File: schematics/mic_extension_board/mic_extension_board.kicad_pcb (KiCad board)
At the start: 2 copper layers, 103.5 x 88.9 mm, 56 parts, among them J1 XLR3, J2 Power, J3 Aux In, J4 I2C Bus, J5 6Pin ISP, J6 Input/Output, J7 XLR3, J8 XLR3, SW1 Stompbutton 1, SW2 Stompbutton 2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

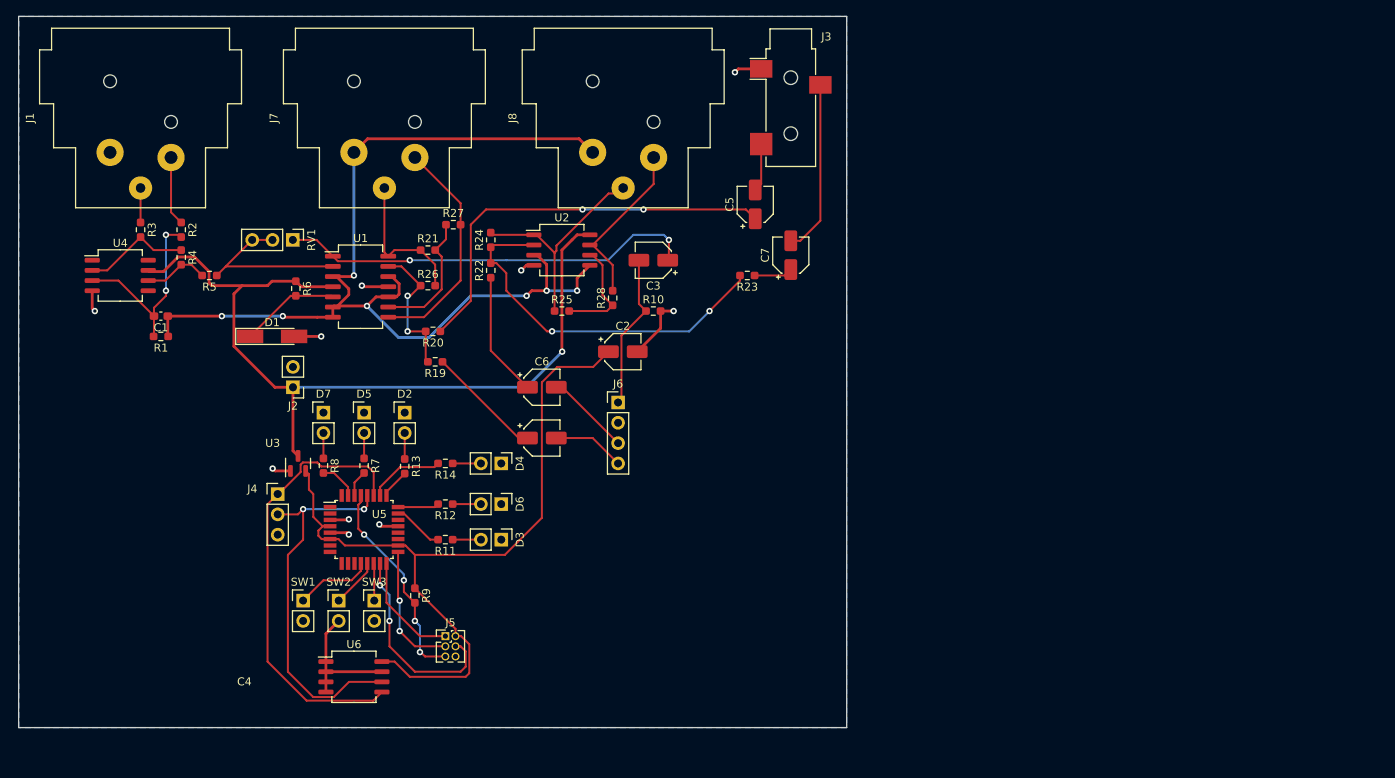
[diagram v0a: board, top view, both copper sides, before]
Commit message: corrected ic footprints, shrinked
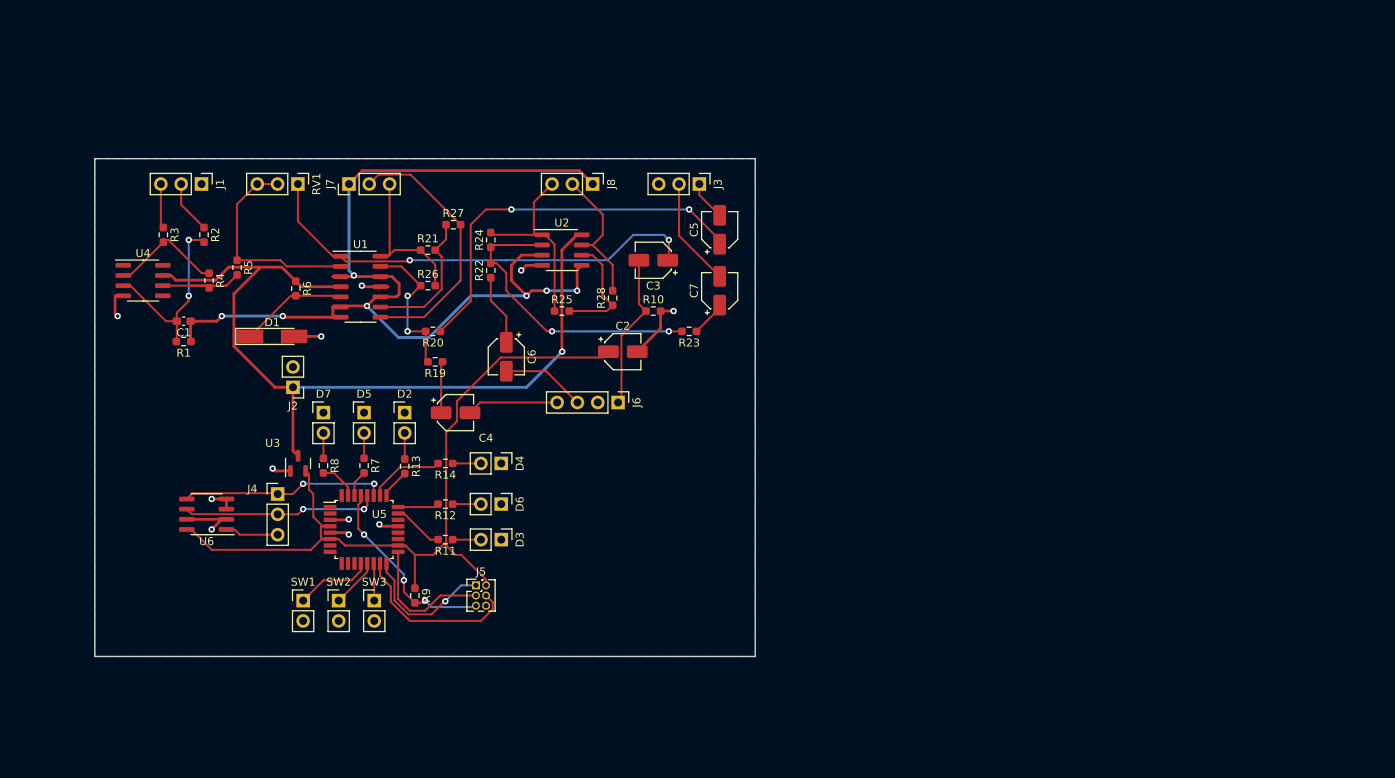
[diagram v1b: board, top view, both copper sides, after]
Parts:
- J1: footprint Connector_Audio:Jack_XLR_Neutrik_NC3FAAH-0_Horizontal -> Connector_PinHeader_2.54mm:PinHeader_1x03_P2.54mm_Vertical
- J3: footprint Connector_Audio:Jack_3.5mm_CUI_SJ-3523-SMT_Horizontal -> Connector_PinHeader_2.54mm:PinHeader_1x03_P2.54mm_Vertical
- J7, J8: footprint Connector_Audio:Jack_XLR_Neutrik_NC3FAAH1-0_Horizontal -> Connector_PinHeader_2.54mm:PinHeader_1x03_P2.54mm_Vertical
- U1: footprint Package_SO:SO-14_5.3x10.2mm_P1.27mm -> Package_SO:SOIC-14_3.9x8.7mm_P1.27mm
- U2, U4, U6: footprint Package_SO:SO-8_5.3x6.2mm_P1.27mm -> Package_SO:SOIC-8_3.9x4.9mm_P1.27mm
- moved U6 27.4 mm to (48.9, 72.4), turned to 180 degrees
- moved J3 15.7 mm to (110.5, 31.1), turned to -90 degrees
- moved J1 12.1 mm to (48.3, 31.1), turned to -90 degrees
- moved C4 11.3 mm to (80.0, 59.7)
- moved R23 10.1 mm to (109.2, 49.5)
- moved C7 9.94 mm to (113.0, 44.5)
- moved J5 7.41 mm to (82.6, 81.3)
- moved RV1 7.01 mm to (60.3, 31.1)
- moved C6 5.85 mm to (86.4, 52.7), turned to -90 degrees
- moved C5 5.46 mm to (113.0, 36.8)
- moved R4 4.53 mm to (49.2, 43.2)
- moved J7 4.00 mm to (66.7, 31.1)
- moved J8 3.95 mm to (97.2, 31.1), turned to -90 degrees
- moved R5 3.59 mm to (52.7, 41.6), turned to -90 degrees
- moved R2 2.92 mm to (48.6, 37.5)
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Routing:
- net Net-(J4-Pad1): track 55.8 -> 25.8 mm, vias 0 -> 2
- net Net-(J4-Pad2): track 47.9 -> 24.6 mm
- net Net-(R22-Pad2): track 46.7 -> 36.2 mm
- net Net-(C4-Pad1): track 14.6 -> 6.42 mm
- net Net-(C7-Pad2): track 21.7 -> 13.6 mm
- net Net-(C6-Pad1): track 15.6 -> 8.89 mm
- net Net-(J8-Pad3): track 28.6 -> 23.5 mm
- net GND: track 48.8 -> 44.3 mm, vias 10 -> 11
- net Net-(J8-Pad2): track 21.2 -> 16.8 mm
- net Net-(C3-Pad1): track 52.3 -> 56.4 mm
- net Vref: track 130.9 -> 127.1 mm
- net Net-(J7-Pad2): track 28.7 -> 32.4 mm
- net Net-(J5-Pad4): track 25.4 -> 21.7 mm, vias 2 -> 0
- net Net-(J5-Pad1): track 14.0 -> 17.6 mm, vias 0 -> 1
- net Net-(R4-Pad2): track 8.12 -> 11.4 mm
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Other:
- board size 103.5 x 88.9 mm -> 82.5 x 62.2 mm

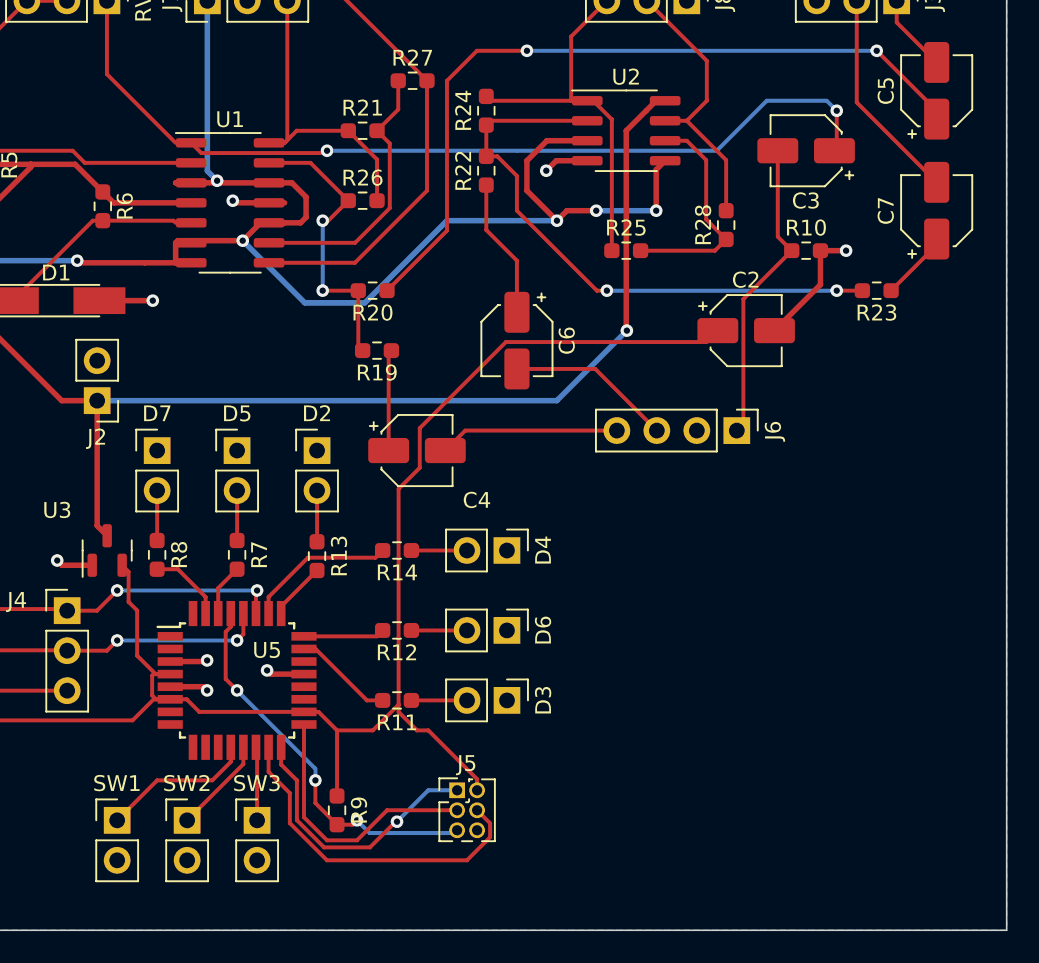
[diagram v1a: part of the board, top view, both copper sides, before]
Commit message: added headphone amp
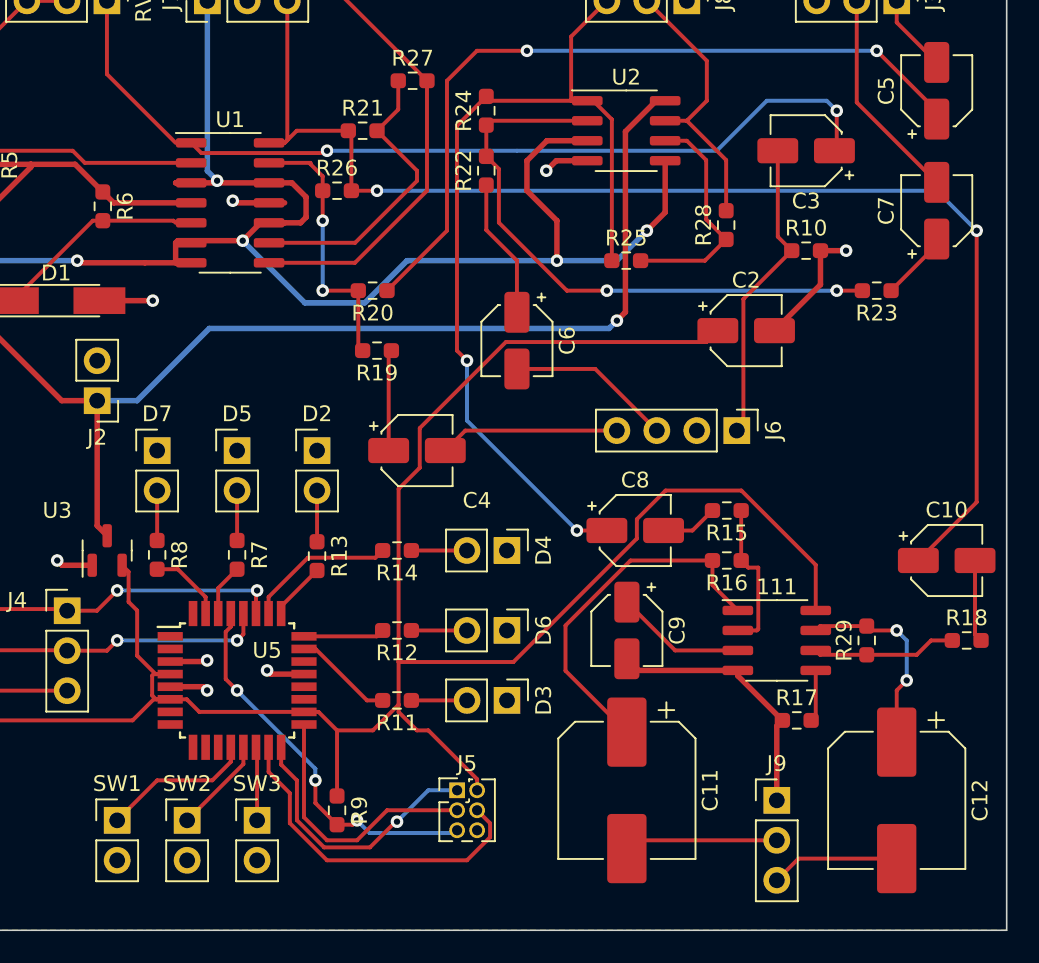
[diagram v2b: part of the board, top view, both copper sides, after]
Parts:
- added 111: LM4881M/NOPB, Package_SO:SOIC-8_3.9x4.9mm_P1.27mm, F.Cu at (102.9, 71.8)
- added C10: 0.33uF, Capacitor_SMD:CP_Elec_4x4.5, F.Cu at (113.7, 66.7)
- added C11: 330uF, Capacitor_SMD:CP_Elec_8x10.5, F.Cu at (93.3, 81.3)
- added C12: 330uF, Capacitor_SMD:CP_Elec_8x10.5, F.Cu at (110.5, 81.9)
- added C8: 0.33uF, Capacitor_SMD:CP_Elec_4x4.5, F.Cu at (93.9, 64.8)
- added C9: 1uF, Capacitor_SMD:CP_Elec_4x4.5, F.Cu at (93.3, 71.1)
- added J9: Conn_01x03_Female, Connector_PinHeader_2.54mm:PinHeader_1x03_P2.54mm_Vertical, F.Cu at (102.9, 81.9)
- added R15: 22k, Resistor_SMD:R_0603_1608Metric_Pad0.98x0.95mm_HandSolder, F.Cu at (99.7, 63.5)
- added R16: 22k, Resistor_SMD:R_0603_1608Metric_Pad0.98x0.95mm_HandSolder, F.Cu at (99.7, 66.7)
- added R17: 10k, Resistor_SMD:R_0603_1608Metric_Pad0.98x0.95mm_HandSolder, F.Cu at (104.1, 76.8)
- added R18: 22k, Resistor_SMD:R_0603_1608Metric_Pad0.98x0.95mm_HandSolder, F.Cu at (114.9, 71.8)
- added R29: 22k, Resistor_SMD:R_0603_1608Metric_Pad0.98x0.95mm_HandSolder, F.Cu at (108.6, 71.8)
- moved R26 1.75 mm to (74.9, 43.2)
- moved R25 0.63 mm to (93.3, 47.6)
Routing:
- net Net-(C10-Pad1): track 18.7 -> 80.6 mm, vias 0 -> 2
- net Net-(111-Pad8): track 99.1 -> 135.7 mm
- net Net-(C8-Pad1): track 23.5 -> 57.6 mm, vias 0 -> 2
- net Net-(111-Pad1): track 0.00 -> 23.3 mm
- net GND: track 44.3 -> 61.2 mm
- net Net-(111-Pad7): track 0.00 -> 13.0 mm, vias 0 -> 2
- net Net-(C11-Pad2): track 0.00 -> 9.74 mm
- net Net-(111-Pad2): track 0.00 -> 9.69 mm
- net Net-(111-Pad6): track 0.00 -> 9.17 mm
- net Net-(111-Pad3): track 0.00 -> 8.32 mm
- net Net-(C12-Pad2): track 0.00 -> 8.19 mm
- net Net-(C10-Pad2): track 0.00 -> 5.24 mm
- net Net-(C8-Pad2): track 0.00 -> 3.63 mm
- net Net-(111-Pad5): track 0.00 -> 3.30 mm
- net Vref: track 127.1 -> 130.1 mm, vias 7 -> 6
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
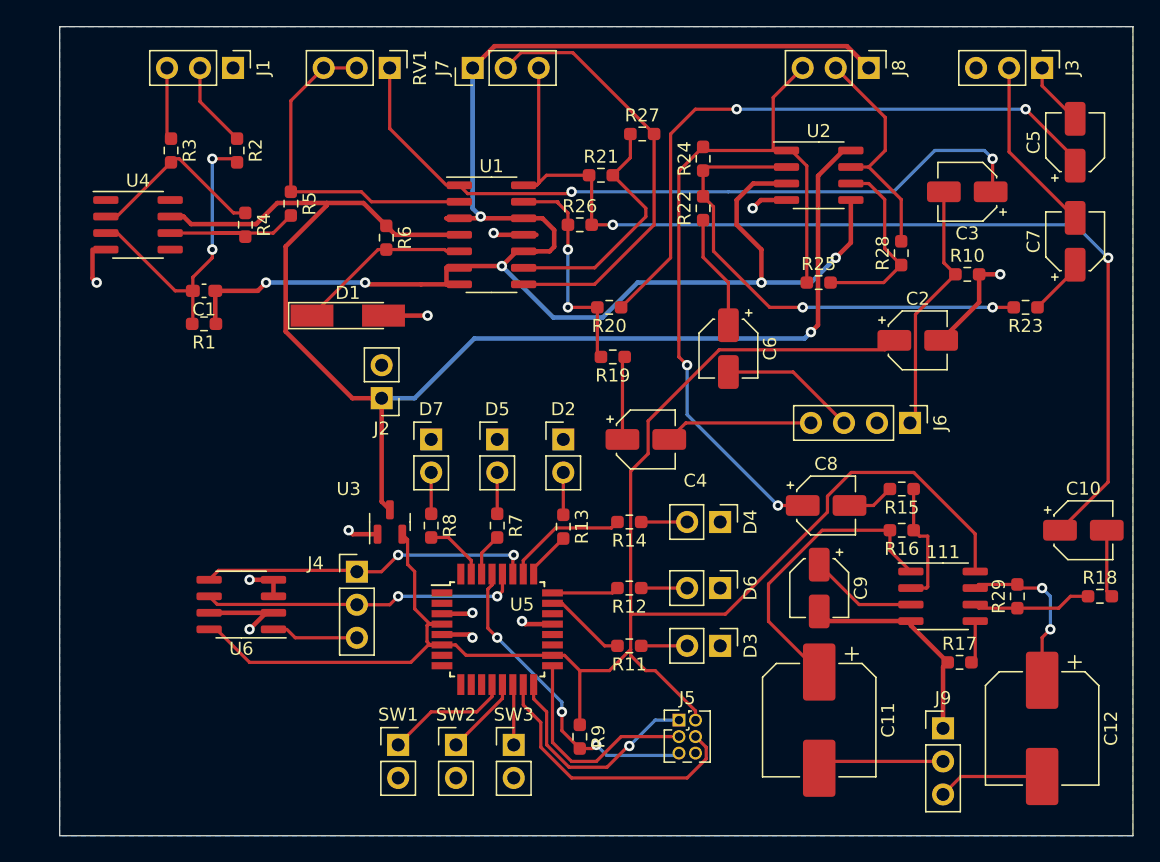
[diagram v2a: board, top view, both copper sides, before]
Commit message: update mic expansion board
the design is now symmetric to the greatest extent, reduces cost
and nasty switch on/off behaviour
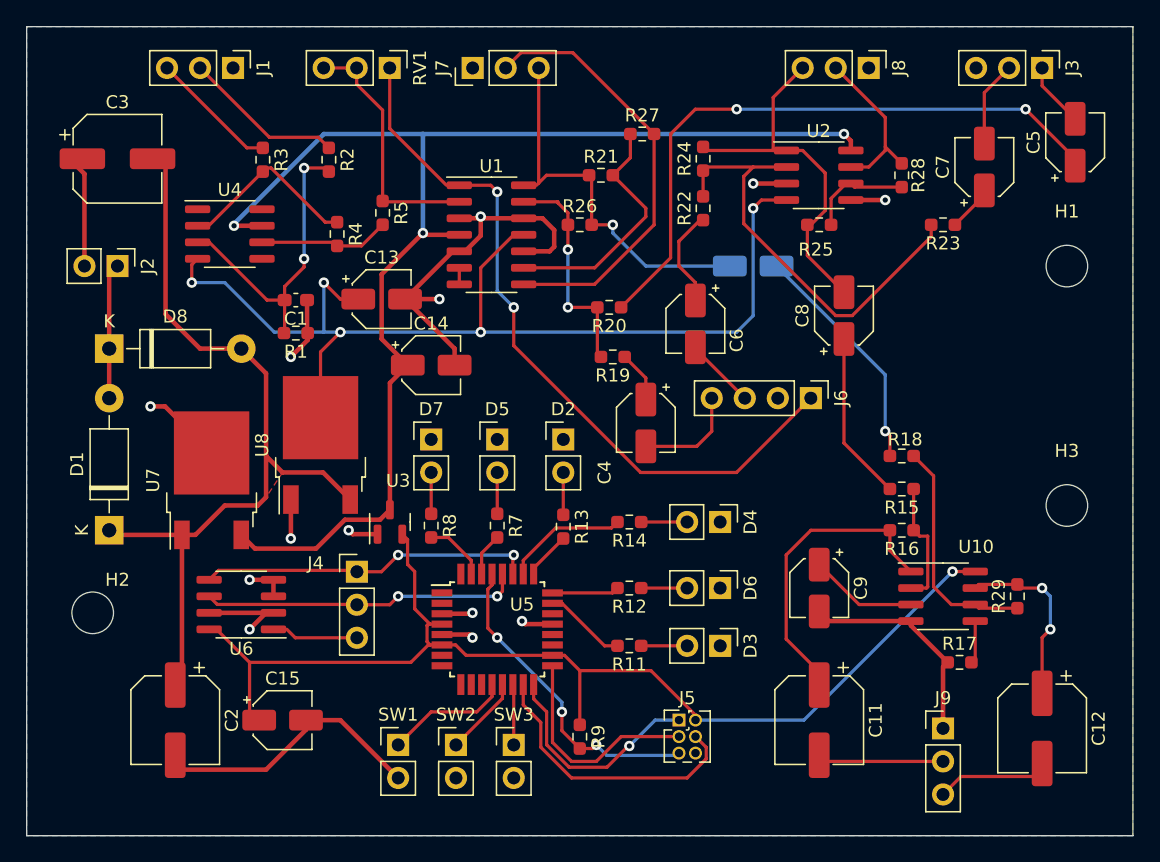
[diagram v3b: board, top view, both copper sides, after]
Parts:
- removed R10: 47k, Resistor_SMD:R_0603_1608Metric_Pad0.98x0.95mm_HandSolder
- removed R6: 1k2, Resistor_SMD:R_0603_1608Metric_Pad0.98x0.95mm_HandSolder
- added C13: 22uF, Capacitor_SMD:CP_Elec_4x4.5, F.Cu at (59.7, 48.9)
- added C14: 22uF, Capacitor_SMD:CP_Elec_4x4.5, F.Cu at (63.5, 54.0)
- added C15: 2.2uF, Capacitor_SMD:CP_Elec_4x4.5, F.Cu at (52.1, 81.3)
- added D8: 1N4001, Diode_THT:D_DO-41_SOD81_P10.16mm_Horizontal, F.Cu at (38.7, 52.7)
- added H1: MountingHole, MountingHole:MountingHole_3.2mm_M3, F.Cu at (112.4, 46.4)
- added H2: MountingHole, MountingHole:MountingHole_3.2mm_M3, F.Cu at (37.5, 73.0)
- added H3: MountingHole, MountingHole:MountingHole_3.2mm_M3, F.Cu at (112.4, 64.8)
- added U7: MC78M05_TO252, Package_TO_SOT_SMD:TO-252-2, F.Cu at (46.6, 62.8)
- added U8: MC79M08_TO252, Package_TO_SOT_SMD:TO-252-2, F.Cu at (55.0, 60.1)
- C10: moved to B.Cu
- C11, C12: footprint Capacitor_SMD:CP_Elec_8x10.5 -> Capacitor_SMD:CP_Elec_6.3x7.7
- C2: value 2.2uF -> 220uF; footprint Capacitor_SMD:CP_Elec_4x4.5 -> Capacitor_SMD:CP_Elec_6.3x7.7
- C3: value 10uF -> 220uF; footprint Capacitor_SMD:CP_Elec_4x4.5 -> Capacitor_SMD:CP_Elec_6.3x7.7
- D1: value 4.7v -> 1N4001; footprint Diode_SMD:D_MiniMELF_Handsoldering -> Diode_THT:D_DO-41_SOD81_P10.16mm_Horizontal
- J2: value Power -> Conn_01x02_Male
- moved C3 65.4 mm to (39.4, 38.1), turned to 0 degrees
- moved C2 64.1 mm to (43.8, 81.3), turned to -90 degrees
- moved C10 32.5 mm to (88.3, 46.4), turned to 180 degrees
- moved D1 24.7 mm to (38.7, 66.7), turned to 90 degrees
- moved J2 22.7 mm to (39.4, 46.4), turned to -90 degrees
- moved R18 18.7 mm to (99.7, 61.0), turned to 180 degrees
- moved C8 14.7 mm to (95.2, 50.2), turned to 90 degrees
- moved C7 9.03 mm to (106.0, 38.7)
- moved R23 8.98 mm to (102.9, 43.2)
- moved J6 7.86 mm to (92.7, 56.5)
- moved C1 7.10 mm to (53.1, 49.0)
- moved R1 7.10 mm to (53.1, 51.5)
- moved R2 7.10 mm to (55.6, 38.2)
- moved R3 7.10 mm to (50.6, 38.2)
- moved R4 7.10 mm to (56.3, 43.9)
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- renumbered 111 to U10
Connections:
- C1 pad 1: Vref -> GND
- C2 pad 1: Net-(111-Pad8) -> +12V
- C3 pad 1: Net-(C3-Pad1) -> GND
- C3 pad 2: Net-(C3-Pad2) -> +12V
- D1 pad 1: Net-(D1-Pad1) -> +12V
- D1 pad 2: GND -> AC
- J2 pad 1: +9V -> AC
- J5 pad 2: Net-(111-Pad8) -> Net-(C15-Pad1)
- J6 pad 1: Net-(C3-Pad2) -> Net-(J6-Pad1)
- J7 pad 1: Vref -> GND
- J7 pad 3: Net-(C10-Pad1) -> Net-(C10-Pad2)
- J8 pad 1: Vref -> GND
- J8 pad 3: Net-(C8-Pad1) -> Net-(C8-Pad2)
- R1 pad 1: Vref -> GND
- R15 pad 2: Net-(C8-Pad2) -> Net-(C8-Pad1)
- R18 pad 2: Net-(C10-Pad2) -> Net-(C10-Pad1)
- R21 pad 1: Net-(C10-Pad1) -> Net-(C10-Pad2)
- R24 pad 2: Net-(C8-Pad1) -> Net-(C8-Pad2)
- R25 pad 1: Net-(C8-Pad1) -> Net-(C8-Pad2)
- R26 pad 2: Net-(C10-Pad1) -> Net-(C10-Pad2)
- R9 pad 1: Net-(111-Pad8) -> Net-(C15-Pad1)
- RV1 pad 1: Net-(C3-Pad1) -> Net-(J6-Pad1)
- U1 pad 1: Net-(C3-Pad1) -> Net-(J6-Pad1)
- U1 pad 10: Vref -> GND
- U1 pad 11: GND -> -9V
- U1 pad 12: Vref -> GND
- U1 pad 14: Net-(C10-Pad1) -> Net-(C10-Pad2)
- U1 pad 3: Vref -> GND
- U1 pad 5: Net-(D1-Pad1) -> GND
- U1 pad 6: Vref -> Net-(U1-Pad6)
- U1 pad 7: Vref -> Net-(U1-Pad6)
- U10 pad 8: Net-(111-Pad8) -> Net-(C15-Pad1)
- U2 pad 1: Net-(C8-Pad1) -> Net-(C8-Pad2)
- U2 pad 3: Vref -> GND
- U2 pad 4: GND -> -9V
- U2 pad 5: Vref -> GND
- U3 pad 2: Net-(111-Pad8) -> Net-(C15-Pad1)
- U4 pad 4: GND -> -9V
- U5 pad 18: Net-(111-Pad8) -> Net-(C15-Pad1)
- U5 pad 4: Net-(111-Pad8) -> Net-(C15-Pad1)
- U5 pad 6: Net-(111-Pad8) -> Net-(C15-Pad1)
- U6 pad 8: Net-(111-Pad8) -> Net-(C15-Pad1)
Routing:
- net Net-(111-Pad8): track 135.7 -> 0.00 mm
- net Vref: track 130.1 -> 0.00 mm, vias 6 -> 0
- net Net-(C15-Pad1): track 0.00 -> 86.8 mm, vias 0 -> 1
- net -9V: track 0.00 -> 81.1 mm, vias 0 -> 5
- net +12V: track 0.00 -> 62.6 mm
- net Net-(C10-Pad1): track 80.6 -> 18.2 mm, vias 2 -> 1
- net GND: track 61.2 -> 119.9 mm, vias 11 -> 13
- net Net-(C3-Pad1): track 56.4 -> 0.00 mm, vias 2 -> 0
- net Net-(J6-Pad1): track 0.00 -> 55.6 mm, vias 0 -> 2
- net Net-(C8-Pad1): track 57.6 -> 13.0 mm, vias 2 -> 0
- net Net-(C10-Pad2): track 5.24 -> 29.1 mm, vias 0 -> 1
- net Net-(C8-Pad2): track 3.63 -> 27.2 mm
- net Net-(C3-Pad2): track 19.6 -> 0.00 mm
- net Net-(D1-Pad1): track 12.5 -> 0.00 mm
- net AC: track 0.00 -> 9.52 mm
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- added copper zone on F.Cu, net +12V
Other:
- board size 82.5 x 62.2 mm -> 85.1 x 62.2 mm
